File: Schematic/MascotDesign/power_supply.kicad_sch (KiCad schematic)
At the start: 7 parts, among them J1 Charger input, J2 LCD power USB, J3 LCD power USB, J4 PI power USB, U1 Generic_Buck_Regulator, U2 Generic_Buck_Regulator

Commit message: Work on power supply schematic
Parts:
- added SW1: Main power cutoff, symbol Switch:SW_SPDT
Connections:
- net +12V: now also SW1.2 (B); no longer U1.1 (GND), U2.1 (GND)
- net GND: now also U1.1 (GND), U1.3 (GND), U2.1 (GND), U2.3 (GND); no longer U1.2 (IN), U1.4 (OUT), U2.2 (IN), U2.4 (OUT)
- net LCD 5v5: now also U1.4 (OUT); no longer U1.3 (GND)
- net PI 5v5: now also U2.4 (OUT); no longer U2.3 (GND)
- new net AMP POWER IN: SW1.1 (A), U1.2 (IN), U2.2 (IN)
- no-connect marks 6 -> 7
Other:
- moved on the sheet: J1, J2, J3, J4, U1, U2

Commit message: Assign footprints and begin PCB layout
Need to check the ECE shop to see what parts we have on hand before we get too far into this, but still.
It's a start.
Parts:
- BT1: footprint (none) -> TerminalBlock_RND:TerminalBlock_RND_205-00001_1x02_P5.00mm_Horizontal
- J1: footprint (none) -> Connector_PinHeader_2.54mm:PinHeader_1x02_P2.54mm_Vertical
- J2: renamed from J4; footprint (none) -> Connector_PinHeader_2.54mm:PinHeader_1x04_P2.54mm_Vertical
- J3: footprint (none) -> Connector_PinHeader_2.54mm:PinHeader_1x04_P2.54mm_Vertical
- J4: renamed from J2; footprint (none) -> Connector_PinHeader_2.54mm:PinHeader_1x04_P2.54mm_Vertical
- SW1: footprint (none) -> My_Library:SK12D07VG4
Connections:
- net AMP POWER IN renamed 12V SWITCHED
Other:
- title: (none) -> Power Supply Subsystem

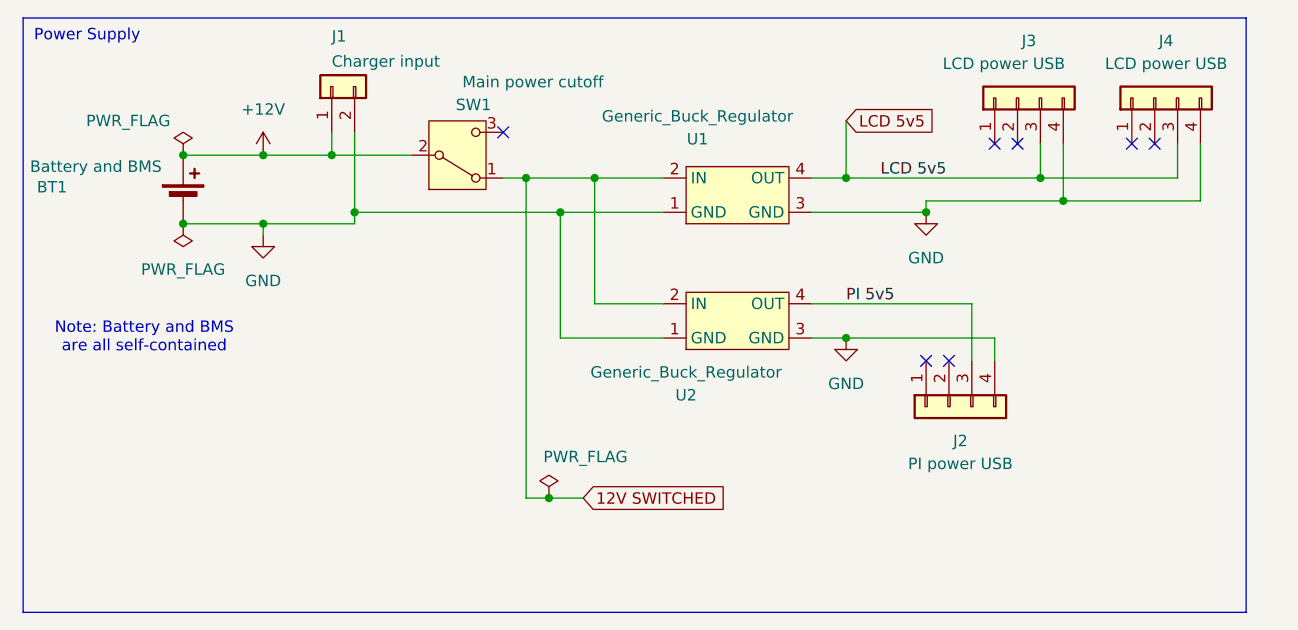
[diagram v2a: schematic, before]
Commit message: Work on CAD and schematics
Got most of the components modeled for reference, now arranging them and creating brackets
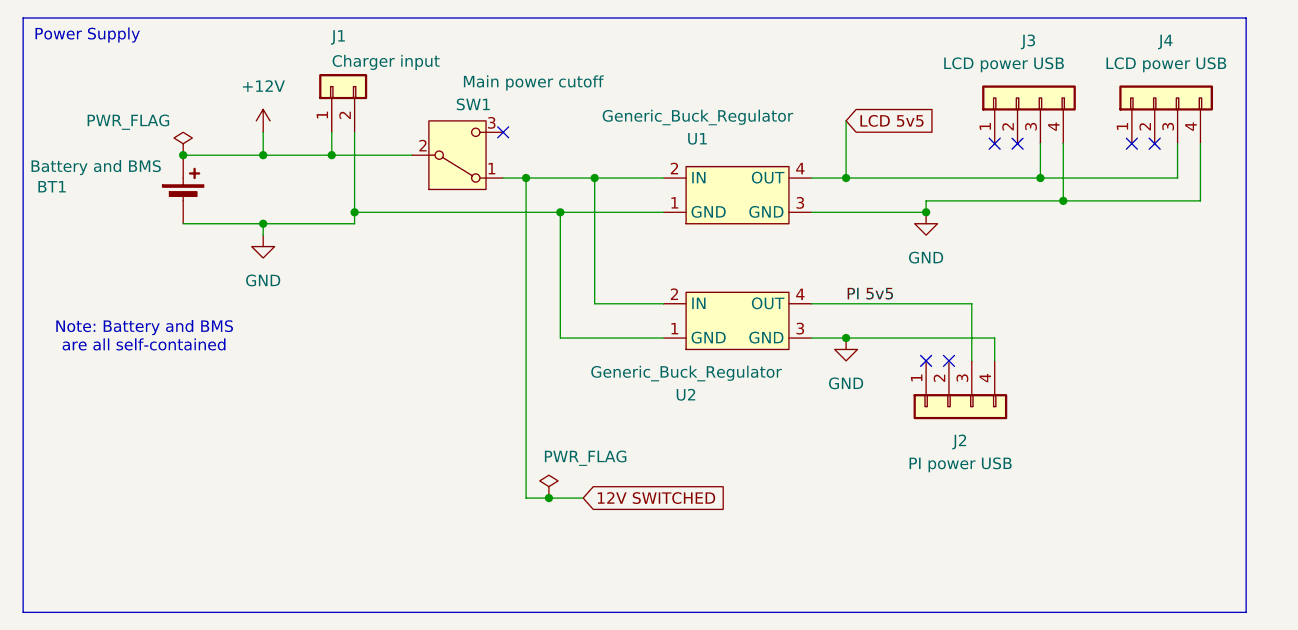
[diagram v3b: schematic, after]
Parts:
- U1, U2: footprint My_Library:Generic Buck Regulator -> TerminalBlock_RND:TerminalBlock_RND_205-00003_1x04_P5.00mm_Horizontal
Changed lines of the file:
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@@
-	)
-	(junction
-		(at 39.37 41.91)
-		(diameter 0)
-		(color 0 0 0 0)
 	)
 	(junction
@@
 	(wire
 		(pts
+			(xy 48.26 31.75) (xy 48.26 34.29)
+		)
+		(stroke
+			(width 0)
+			(type default)
+		)
+	)
+	(wire
+		(pts
 			(xy 85.09 36.83) (xy 77.47 36.83)
 		)
@@
 	(label "PI 5v5"
 		(at 113.03 50.8 0)
-		(effects
-			(font
-				(size 1.27 1.27)
-			)
-			(justify left bottom)
-		)
-	)
-	(label "LCD 5v5"
-		(at 116.84 36.83 0)
 		(effects
 			(font
@@
 			)
 		)
-		(property "Footprint" "My_Library:Generic Buck Regulator"
+		(property "Footprint" "TerminalBlock_RND:TerminalBlock_RND_205-00003_1x04_P5.00mm_Horizontal"
 			(at 100.33 48.26 0)
 			(effects
@@
 			)
 		)
-		(property "Footprint" "My_Library:Generic Buck Regulator"
+		(property "Footprint" "TerminalBlock_RND:TerminalBlock_RND_205-00003_1x04_P5.00mm_Horizontal"
 			(at 100.33 62.23 0)
 			(effects
@@
 	(symbol
 		(lib_id "power:+12V")
-		(at 48.26 34.29 0)
+		(at 48.26 31.75 0)
 		(unit 1)
 		(exclude_from_sim no)
@@
 		(fields_autoplaced yes)
 		(property "Reference" "#PWR04"
-			(at 48.26 38.1 0)
+			(at 48.26 35.56 0)
 			(effects
 				(font
@@
 		)
 		(property "Value" "+12V"
-			(at 48.26 29.21 0)
+			(at 48.26 26.67 0)
 			(effects
 				(font
@@
 		)
 		(property "Footprint" ""
-			(at 48.26 34.29 0)
+			(at 48.26 31.75 0)
 			(effects
 				(font
@@
 		)
 		(property "Datasheet" ""
-			(at 48.26 34.29 0)
+			(at 48.26 31.75 0)
 			(effects
 				(font
@@
 		)
 		(property "Description" "Power symbol creates a global label with name \"+12V\""
-			(at 48.26 34.29 0)
+			(at 48.26 31.75 0)
 			(effects
 				(font
@@
 					(unit 1)
 				)
-			)
-		)
-	)
-	(symbol
-		(lib_id "power:PWR_FLAG")
-		(at 39.37 41.91 180)
-		(unit 1)
-		(exclude_from_sim no)
-		(in_bom yes)
-		(on_board yes)
-		(dnp no)
-		(fields_autoplaced yes)
-		(property "Reference" "#FLG02"
-			(at 39.37 43.815 0)
-			(effects
-				(font
-					(size 1.27 1.27)
-				)
-				(hide yes)
-			)
-		)
-		(property "Value" "PWR_FLAG"
-			(at 39.37 46.99 0)
-			(effects
-				(font
-					(size 1.27 1.27)
-				)
-			)
-		)
-		(property "Footprint" ""
-			(at 39.37 41.91 0)
-			(effects
-				(font
-					(size 1.27 1.27)
-				)
-				(hide yes)
-			)
-		)
-		(property "Datasheet" "~"
-			(at 39.37 41.91 0)
-			(effects
-				(font
-					(size 1.27 1.27)
-				)
-				(hide yes)
-			)
-		)
-		(property "Description" "Special symbol for telling ERC where power comes from"
-			(at 39.37 41.91 0)
-			(effects
-				(font
-					(size 1.27 1.27)
-				)
-				(hide yes)
-			)
-		)
-		(pin "1"
-		)
-		(instances
-			(project "MascotDesign"
-				(path "/ba045f6c-d730-41b1-992e-d77c9aee61c5/621dc98a-3a96-4433-a17f-2055bce50a9c"
-					(reference "#FLG02")
-					(unit 1)
-				)

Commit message: Do PCB layout
I need to check our cap footprints to make sure we got the right ones.
Other than that, the PCB should be mostly routed.
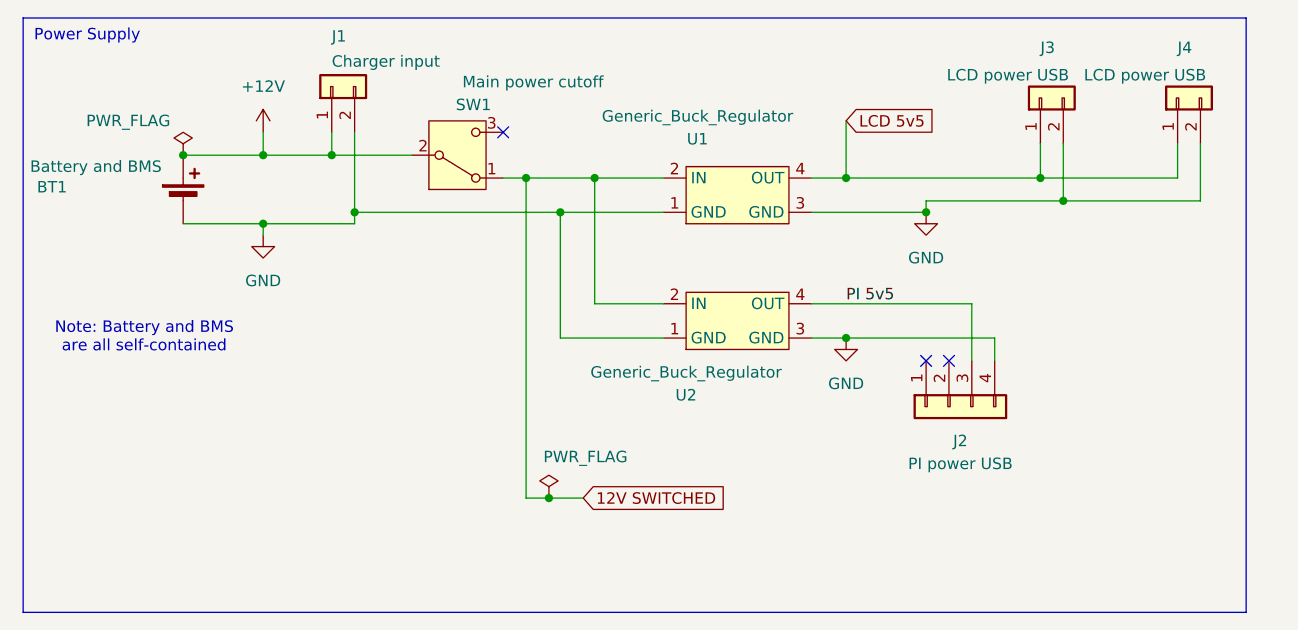
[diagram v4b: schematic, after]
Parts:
- removed J3, J4: LCD power USB, Connector_PinHeader_2.54mm:PinHeader_1x04_P2.54mm_Vertical, symbol Connector_Generic:Conn_01x04
- added J3, J4: LCD power USB, Connector_PinHeader_2.54mm:PinHeader_1x02_P2.54mm_Vertical, symbol Connector_Generic:Conn_01x02
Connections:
- net GND: now also J3.2 (Pin_2), J4.2 (Pin_2)
- net LCD 5v5: now also J3.1 (Pin_1), J4.1 (Pin_1)
- no-connect marks 7 -> 3
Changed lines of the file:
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@@
-	)
-	(no_connect
-		(at 144.78 33.02)
-	)
-	(no_connect
-		(at 147.32 33.02)
-	)
-	(no_connect
-		(at 129.54 33.02)
 	)
 	(no_connect
@@
 	)
 	(no_connect
-		(at 132.08 33.02)
-	)
-	(no_connect
 		(at 121.92 57.15)
 	)
@@
 	(wire
 		(pts
-			(xy 80.01 72.39) (xy 83.82 72.39)
-		)
-		(stroke
-			(width 0)
-			(type default)
-		)
-	)
-	(wire
-		(pts
 			(xy 149.86 33.02) (xy 149.86 36.83)
 		)
@@
 		(pts
 			(xy 109.22 36.83) (xy 113.03 36.83)
+		)
+		(stroke
+			(width 0)
+			(type default)
+		)
+	)
+	(wire
+		(pts
+			(xy 83.82 72.39) (xy 80.01 72.39)
 		)
 		(stroke
@@
 	(symbol
 		(lib_id "Connector_Generic:Conn_01x02")
+		(at 149.86 27.94 90)
+		(unit 1)
+		(exclude_from_sim no)
+		(in_bom yes)
+		(on_board yes)
+		(dnp no)
+		(property "Reference" "J4"
+			(at 149.86 22.352 90)
+			(effects
+				(font
+					(size 1.27 1.27)
+				)
+				(justify right)
+			)
+		)
+		(property "Value" "LCD power USB"
+			(at 139.446 25.4 90)
+			(effects
+				(font
+					(size 1.27 1.27)
+				)
+				(justify right)
+			)
+		)
+		(property "Footprint" "Connector_PinHeader_2.54mm:PinHeader_1x02_P2.54mm_Vertical"
+			(at 149.86 27.94 0)
+			(effects
+				(font
+					(size 1.27 1.27)
+				)
+				(hide yes)
+			)
+		)
+		(property "Datasheet" "~"
+			(at 149.86 27.94 0)
+			(effects
+				(font
+					(size 1.27 1.27)
+				)
+				(hide yes)
+			)
+		)
+		(property "Description" "Generic connector, single row, 01x02, script generated (kicad-library-utils/schlib/autogen/connector/)"
+			(at 149.86 27.94 0)
+			(effects
+				(font
+					(size 1.27 1.27)
+				)
+				(hide yes)
+			)
+		)
+		(pin "2"
+		)
+		(pin "1"
+		)
+		(instances
+			(project "MascotDesign"
+				(path "/ba045f6c-d730-41b1-992e-d77c9aee61c5/621dc98a-3a96-4433-a17f-2055bce50a9c"
+					(reference "J4")
+					(unit 1)
+				)
+			)
+		)
+	)
+	(symbol
+		(lib_id "Connector_Generic:Conn_01x02")
 		(at 55.88 26.67 90)
 		(unit 1)
@@
 	(symbol
 		(lib_id "Connector_Generic:Conn_01x04")
-		(at 132.08 27.94 90)
-		(unit 1)
-		(exclude_from_sim no)
-		(in_bom yes)
-		(on_board yes)
-		(dnp no)
-		(property "Reference" "J3"
-			(at 133.35 21.59 90)
-			(effects
-				(font
-					(size 1.27 1.27)
-				)
-			)
-		)
-		(property "Value" "LCD power USB"
-			(at 130.556 24.13 90)
-			(effects
-				(font
-					(size 1.27 1.27)
-				)
-			)
-		)
-		(property "Footprint" "Connector_PinHeader_2.54mm:PinHeader_1x04_P2.54mm_Vertical"
-			(at 132.08 27.94 0)
-			(effects
-				(font
-					(size 1.27 1.27)
-				)
-				(hide yes)
-			)
-		)
-		(property "Datasheet" "~"
-			(at 132.08 27.94 0)
-			(effects
-				(font
-					(size 1.27 1.27)
-				)
-				(hide yes)
-			)
-		)
-		(property "Description" "Generic connector, single row, 01x04, script generated (kicad-library-utils/schlib/autogen/connector/)"
-			(at 132.08 27.94 0)
-			(effects
-				(font
-					(size 1.27 1.27)
-				)
-				(hide yes)
-			)
-		)
-		(pin "4"
-		)
-		(pin "3"
-		)
-		(pin "2"
-		)
-		(pin "1"
-		)
-		(instances
-			(project "MascotDesign"
-				(path "/ba045f6c-d730-41b1-992e-d77c9aee61c5/621dc98a-3a96-4433-a17f-2055bce50a9c"
-					(reference "J3")
-					(unit 1)
-				)
-			)
-		)
-	)
-	(symbol
-		(lib_id "Connector_Generic:Conn_01x04")
 		(at 124.46 62.23 90)
 		(mirror x)
@@
 				(path "/ba045f6c-d730-41b1-992e-d77c9aee61c5/621dc98a-3a96-4433-a17f-2055bce50a9c"
 					(reference "J2")
+					(unit 1)
+				)
+			)
+		)
+	)
+	(symbol
+		(lib_id "Connector_Generic:Conn_01x02")
+		(at 134.62 27.94 90)
+		(unit 1)
+		(exclude_from_sim no)
+		(in_bom yes)
+		(on_board yes)
+		(dnp no)
+		(property "Reference" "J3"
+			(at 134.62 22.352 90)
+			(effects
+				(font
+					(size 1.27 1.27)
+				)
+				(justify right)
+			)
+		)
+		(property "Value" "LCD power USB"
+			(at 124.206 25.4 90)
+			(effects
+				(font
+					(size 1.27 1.27)
+				)
+				(justify right)
+			)
+		)
+		(property "Footprint" "Connector_PinHeader_2.54mm:PinHeader_1x02_P2.54mm_Vertical"
+			(at 134.62 27.94 0)
+			(effects
+				(font
+					(size 1.27 1.27)
+				)
+				(hide yes)
+			)
+		)
+		(property "Datasheet" "~"
+			(at 134.62 27.94 0)
+			(effects
+				(font
+					(size 1.27 1.27)
+				)
+				(hide yes)
+			)
+		)
+		(property "Description" "Generic connector, single row, 01x02, script generated (kicad-library-utils/schlib/autogen/connector/)"
+			(at 134.62 27.94 0)
+			(effects
+				(font
+					(size 1.27 1.27)
+				)
+				(hide yes)
+			)
+		)
+		(pin "2"
+		)
+		(pin "1"
+		)
+		(instances
+			(project "MascotDesign"
+				(path "/ba045f6c-d730-41b1-992e-d77c9aee61c5/621dc98a-3a96-4433-a17f-2055bce50a9c"
+					(reference "J3")
 					(unit 1)
 				)
@@
 					(unit 1)
 				)
-			)
-		)
-	)
-	(symbol
-		(lib_id "Connector_Generic:Conn_01x04")
-		(at 147.32 27.94 90)
-		(unit 1)
-		(exclude_from_sim no)
-		(in_bom yes)
-		(on_board yes)
-		(dnp no)
-		(fields_autoplaced yes)
-		(property "Reference" "J4"
-			(at 148.59 21.59 90)
-			(effects
-				(font
-					(size 1.27 1.27)
-				)
-			)
-		)
-		(property "Value" "LCD power USB"
-			(at 148.59 24.13 90)
-			(effects
-				(font
-					(size 1.27 1.27)
-				)
-			)
-		)
-		(property "Footprint" "Connector_PinHeader_2.54mm:PinHeader_1x04_P2.54mm_Vertical"
-			(at 147.32 27.94 0)
-			(effects
-				(font
-					(size 1.27 1.27)
-				)
-				(hide yes)
-			)
-		)
-		(property "Datasheet" "~"
-			(at 147.32 27.94 0)
-			(effects
-				(font
-					(size 1.27 1.27)
-				)
-				(hide yes)
-			)
-		)
-		(property "Description" "Generic connector, single row, 01x04, script generated (kicad-library-utils/schlib/autogen/connector/)"
-			(at 147.32 27.94 0)
-			(effects
-				(font
-					(size 1.27 1.27)
-				)
-				(hide yes)
-			)
-		)
-		(pin "4"
-		)
-		(pin "3"
-		)
-		(pin "2"
-		)
-		(pin "1"
-		)
-		(instances
-			(project "MascotDesign"
-				(path "/ba045f6c-d730-41b1-992e-d77c9aee61c5/621dc98a-3a96-4433-a17f-2055bce50a9c"
-					(reference "J4")
-					(unit 1)
-				)

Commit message: update PCB and mounting brackets
give PCB the correct footprints for the parts we have and add more mounting brackets for the 3D model
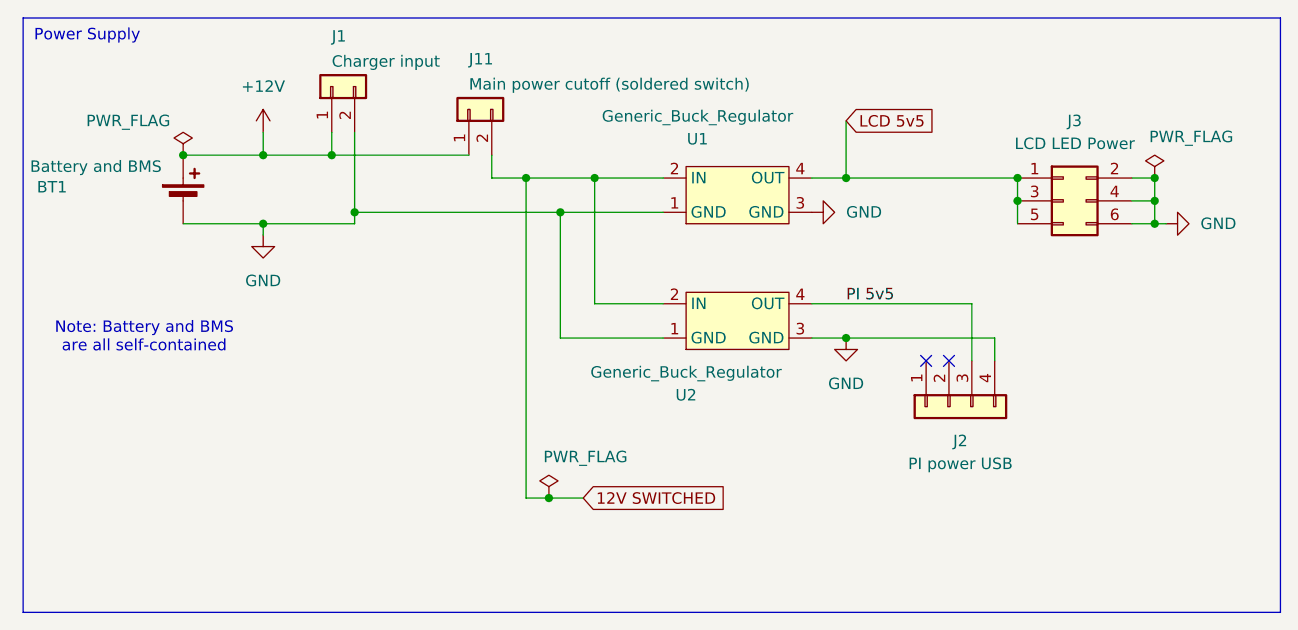
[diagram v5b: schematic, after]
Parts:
- removed J3, J4: LCD power USB, Connector_PinHeader_2.54mm:PinHeader_1x02_P2.54mm_Vertical, symbol Connector_Generic:Conn_01x02
- removed SW1: Main power cutoff, My_Library:SK12D07VG4, symbol Switch:SW_SPDT
- added J11: Main power cutoff (soldered switch), Connector_PinHeader_2.54mm:PinHeader_1x02_P2.54mm_Vertical, symbol Connector_Generic:Conn_01x02
- added J3: LCD LED Power, Connector_PinHeader_2.54mm:PinHeader_2x03_P2.54mm_Vertical, symbol Connector_Generic:Conn_02x03_Odd_Even
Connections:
- net +12V: now also J11.1 (Pin_1)
- net 12V SWITCHED: now also J11.2 (Pin_2)
- net GND: now also J3.2 (Pin_2), J3.4 (Pin_4), J3.6 (Pin_6)
- net LCD 5v5: now also J3.1 (Pin_1), J3.3 (Pin_3), J3.5 (Pin_5)
- no-connect marks 3 -> 2
